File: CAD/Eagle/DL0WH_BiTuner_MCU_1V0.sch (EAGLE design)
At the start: 133 parts, among them Q0321 ABS07-32.768KHZ, U0101 STM32L476RXT_64PIN_LDO, U0601 MC33996, U0701 MC33996, U0801 MC33996, U0921 TS5A23166, U0951 OPA354, U1001 MAX232_SOIC16, U1101 MAX232_SOIC16, U1201 LM53603-Q1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

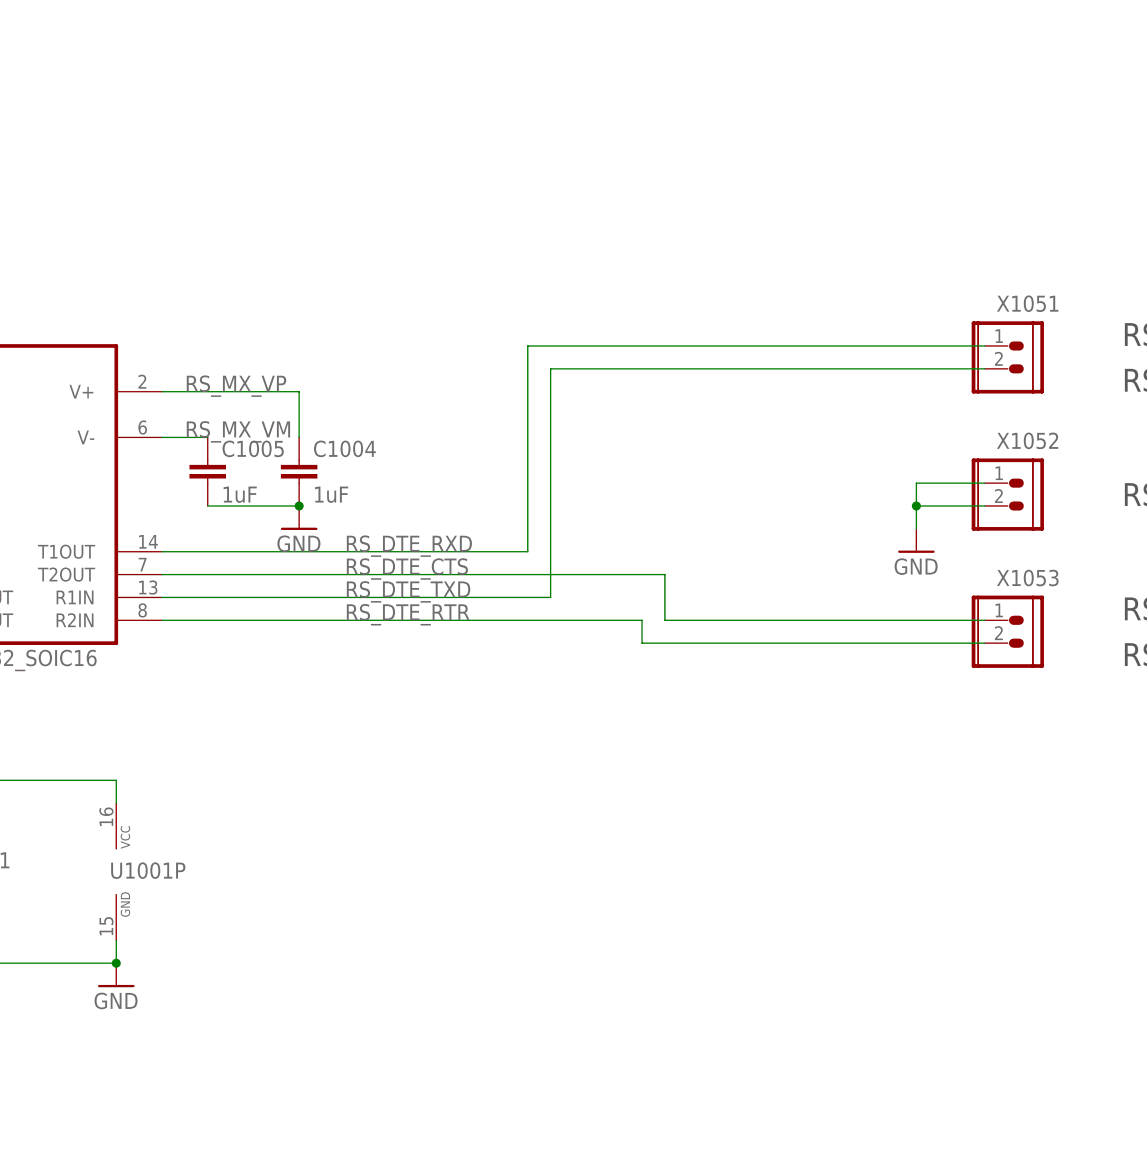
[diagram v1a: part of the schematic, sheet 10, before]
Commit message: HW_1V0 - CAD/Eagle - I/O protection on V24 lines added
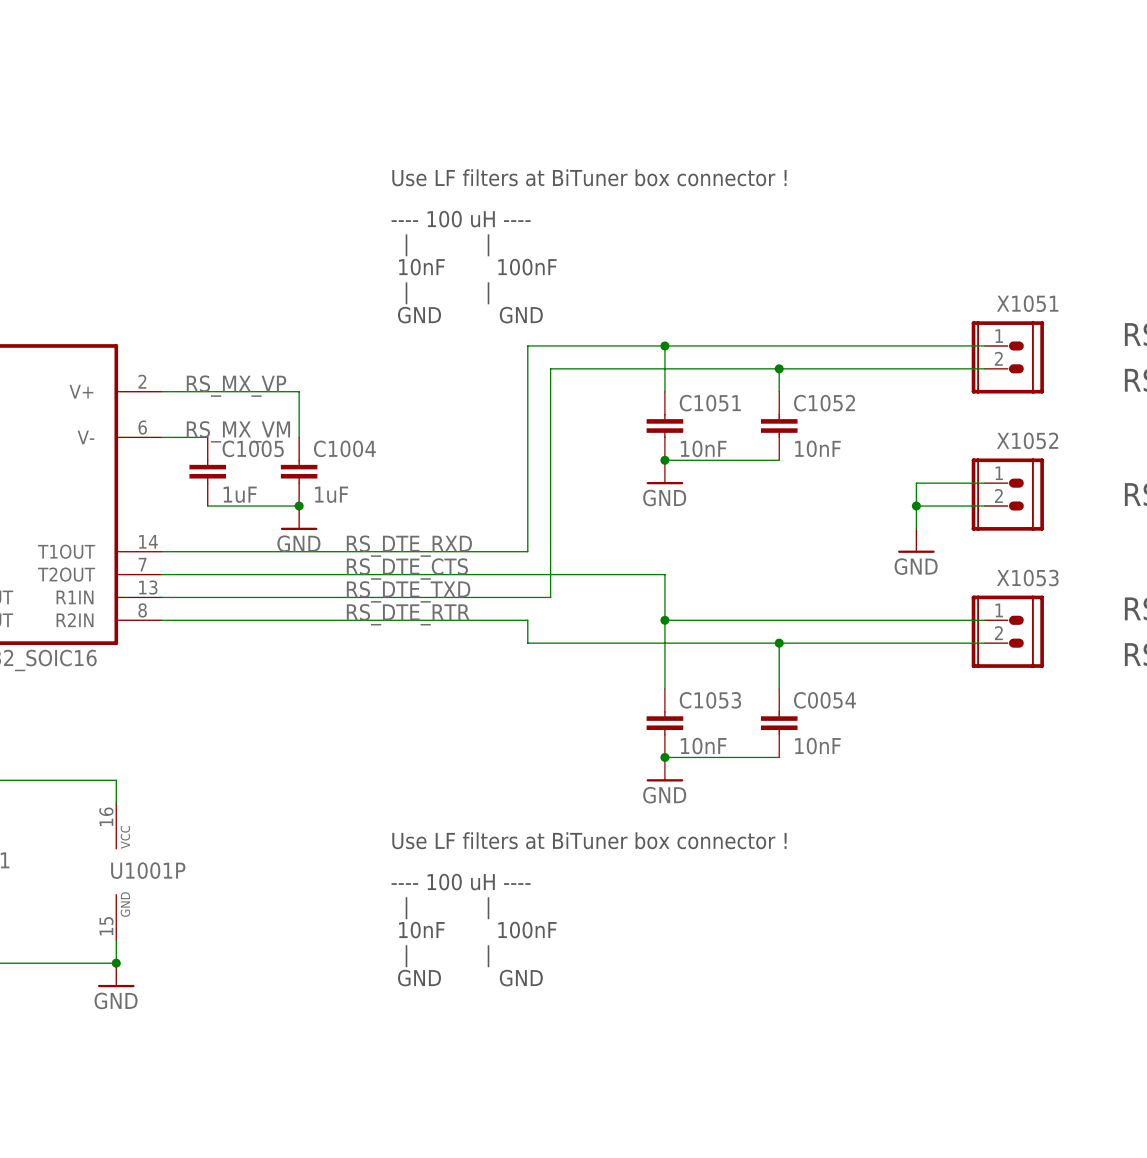
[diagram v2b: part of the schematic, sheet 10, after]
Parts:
- added C0054, C1051, C1052, C1053, C1151, C1152, C1153, C1154: 10nF, df4iah_rcl:C-EUC0603
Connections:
- net CAT_DTE_CTS: now also C1153.1
- net CAT_DTE_RTR: now also C1154.1
- net CAT_DTE_RXD: now also C1151.1
- net CAT_DTE_TXD: now also C1152.1
- net GND: now also C0054.2, C1051.2, C1052.2, C1053.2, C1151.2, C1152.2, C1153.2, C1154.2
- net RS_DTE_CTS: now also C1053.1
- net RS_DTE_RTR: now also C0054.1
- net RS_DTE_RXD: now also C1051.1
- net RS_DTE_TXD: now also C1052.1
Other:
- note added: "---- 100 uH ---- | | 10nF 100nF | | GND GND"
- note added: "Use LF filters at BiTuner box connector !"
